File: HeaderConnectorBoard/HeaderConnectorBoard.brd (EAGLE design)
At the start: 31.1 x 68.6 mm, 2 parts

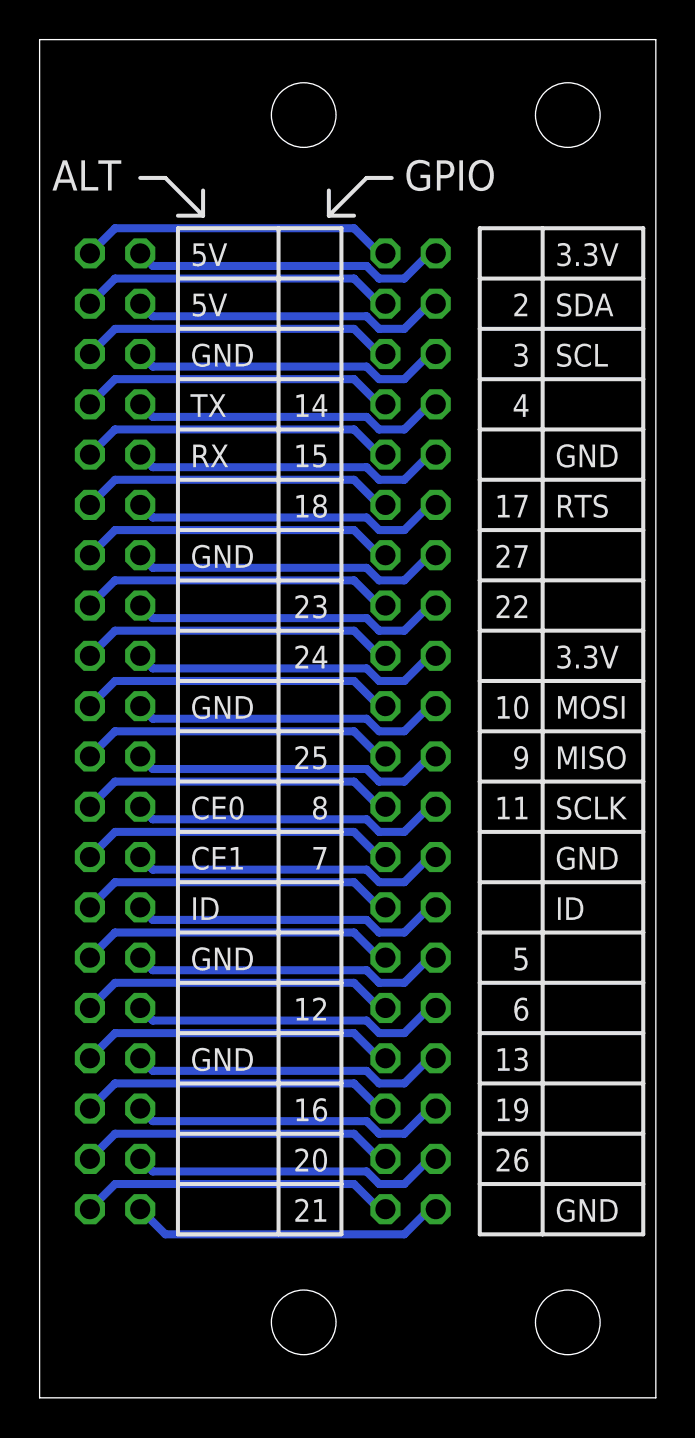
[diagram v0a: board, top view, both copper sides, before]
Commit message: Lid conn - added POWER LED
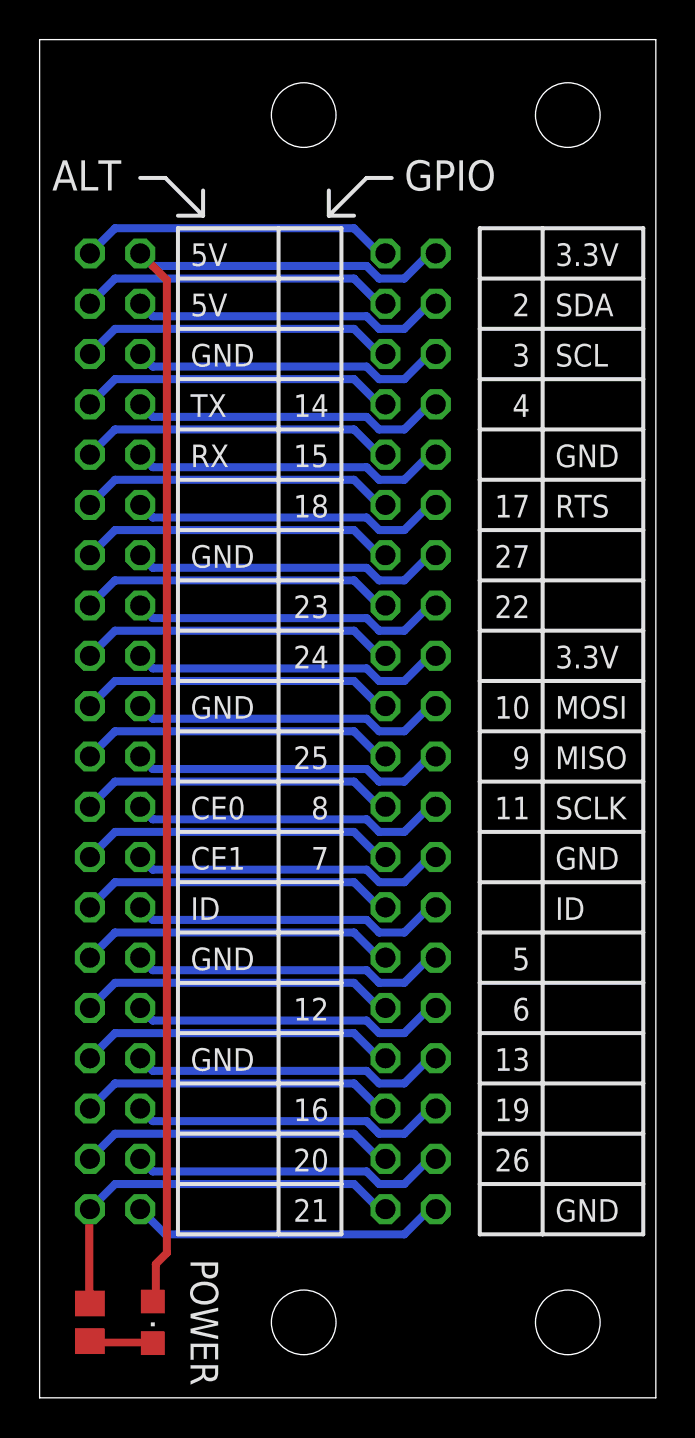
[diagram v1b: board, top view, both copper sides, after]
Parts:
- added LED1: 475-1410-2-ND, led:CHIPLED_0805
- added R1: 200, resistor:R0805
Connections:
- new net N$1: LED1.C, R1.2
- net 5V_2: now also LED1.A
- net GND6: now also R1.1
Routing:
- net 5V_2: track 16.0 -> 69.7 mm
- net GND6: track 16.0 -> 20.8 mm
- net N$1: track 0.00 -> 3.19 mm
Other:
- board text added: "POWER"
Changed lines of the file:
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@@
 <?xml version="1.0" encoding="utf-8"?>
 <!DOCTYPE eagle SYSTEM "eagle.dtd">
-<eagle version="7.1.0">
+<eagle version="7.6.0">
 <drawing>
 <settings>
@@
 <layer number="2" name="Route2" color="1" fill="3" visible="yes" active="yes"/>
 <layer number="3" name="Route3" color="4" fill="3" visible="yes" active="yes"/>
+<layer number="4" name="Route4" color="1" fill="4" visible="no" active="no"/>
+<layer number="5" name="Route5" color="4" fill="4" visible="no" active="no"/>
+<layer number="6" name="Route6" color="1" fill="8" visible="no" active="no"/>
+<layer number="7" name="Route7" color="4" fill="8" visible="no" active="no"/>
+<layer number="8" name="Route8" color="1" fill="2" visible="no" active="no"/>
+<layer number="9" name="Route9" color="4" fill="2" visible="no" active="no"/>
+<layer number="10" name="Route10" color="1" fill="7" visible="no" active="no"/>
+<layer number="11" name="Route11" color="4" fill="7" visible="no" active="no"/>
+<layer number="12" name="Route12" color="1" fill="5" visible="no" active="no"/>
+<layer number="13" name="Route13" color="4" fill="5" visible="no" active="no"/>
 <layer number="14" name="Route14" color="1" fill="6" visible="yes" active="yes"/>
 <layer number="15" name="Route15" color="4" fill="6" visible="yes" active="yes"/>
@@
 <layer number="97" name="Info" color="7" fill="1" visible="no" active="no"/>
 <layer number="98" name="Guide" color="6" fill="1" visible="no" active="no"/>
+<layer number="99" name="SpiceOrder" color="5" fill="1" visible="no" active="no"/>
 </layers>
 <board>
@@
 <wire x1="8.255" y1="59.69" x2="6.35" y2="61.595" width="0.2032" layer="21"/>
 <wire x1="6.35" y1="61.595" x2="5.08" y2="61.595" width="0.2032" layer="21"/>
+<text x="7.62" y="3.81" size="1.397" layer="21" font="vector" rot="SR270" align="bottom-center">POWER</text>
 </plain>
 <attributes>
@@
 <attribute name="VALUE" x="-0.635" y="59.055" size="1.27" layer="27" rot="R270"/>
 </element>
+<element name="LED1" library="led" package="CHIPLED_0805" value="475-1410-2-ND" x="5.715" y="3.81" smashed="yes" rot="R180"/>
+<element name="R1" library="resistor" package="R0805" value="200" x="2.54" y="3.81" smashed="yes" rot="R270"/>
 </elements>
 <signals>
@@
 <wire x1="19.685" y1="57.785" x2="18.415" y2="56.515" width="0.4064" layer="16"/>
 <wire x1="19.685" y1="57.785" x2="20.0025" y2="57.785" width="0.4064" layer="16"/>
+<contactref element="LED1" pad="A"/>
+<wire x1="5.8674" y1="6.7564" x2="5.8674" y2="5.0292" width="0.4064" layer="1"/>
+<wire x1="6.4262" y1="7.3152" x2="5.8674" y2="6.7564" width="0.4064" layer="1"/>
+<wire x1="6.4262" y1="56.4388" x2="6.4262" y2="7.3152" width="0.4064" layer="1"/>
+<wire x1="5.08" y1="57.785" x2="6.4262" y2="56.4388" width="0.4064" layer="1"/>
+<wire x1="5.8674" y1="5.0292" x2="5.715" y2="4.86" width="0.4064" layer="1"/>
 </signal>
 <signal name="5V_1">
@@
 <wire x1="17.145" y1="9.525" x2="15.875" y2="10.795" width="0.4064" layer="16"/>
 <wire x1="17.145" y1="9.525" x2="17.4625" y2="9.525" width="0.4064" layer="16"/>
+<contactref element="R1" pad="1"/>
+<wire x1="2.5146" y1="9.4996" x2="2.5146" y2="5.0292" width="0.4064" layer="1"/>
+<wire x1="2.5146" y1="5.0292" x2="2.54" y2="4.76" width="0.4064" layer="1"/>
+<wire x1="2.5146" y1="9.4996" x2="2.54" y2="9.525" width="0.4064" layer="1"/>
 </signal>
 <signal name="21">
@@
 <wire x1="19.685" y1="24.765" x2="20.0025" y2="24.765" width="0.4064" layer="16"/>
 </signal>
+<signal name="N$1">
+<contactref element="LED1" pad="C"/>
+<contactref element="R1" pad="2"/>
+<wire x1="2.794" y1="2.794" x2="5.588" y2="2.794" width="0.4064" layer="1"/>
+<wire x1="5.588" y1="2.794" x2="5.715" y2="2.76" width="0.4064" layer="1"/>
+<wire x1="2.794" y1="2.794" x2="2.54" y2="2.86" width="0.4064" layer="1"/>
+</signal>
 </signals>
